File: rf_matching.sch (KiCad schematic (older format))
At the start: 12 parts, among them J1 RFI, J2 RFO, J3 CTRL, J4 ANT, J5 3V3, U1 pe4259ds, U2 SF2098

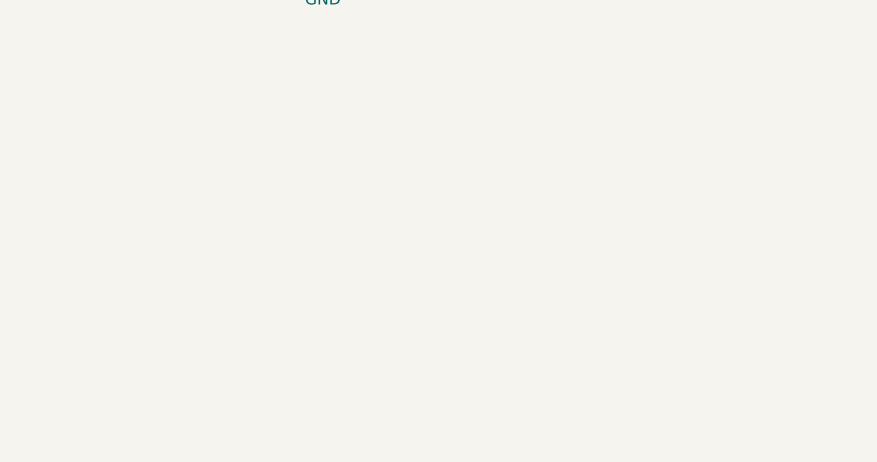
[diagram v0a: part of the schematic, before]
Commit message: Add thicker bias, add PCB LOSS line
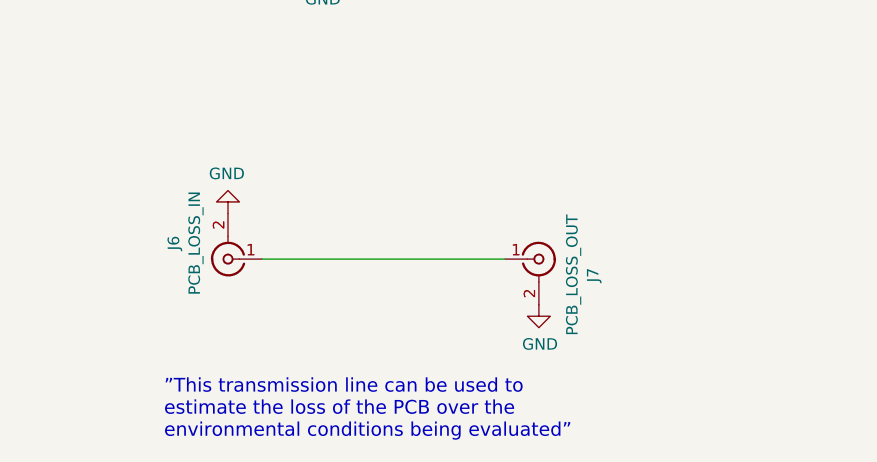
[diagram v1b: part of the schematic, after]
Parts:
- added J6: PCB_LOSS_IN, KiCad/Connectors_Molex.pretty:Molex_SMA_Jack_Edge_Mount, symbol Conn_Coaxial
- added J7: PCB_LOSS_OUT, KiCad/Connectors_Molex.pretty:Molex_SMA_Jack_Edge_Mount, symbol Conn_Coaxial
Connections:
- net GND: now also J6.2 (Ext), J7.2 (Ext)
- new net: J6.1 (In), J7.1 (In)
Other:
- note added: "”This transmission line can be used to \nestimate the loss of the PCB over the \nenvironmental conditions being evaluated”"
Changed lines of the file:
@@
 Wire Wire Line
 	3320 3680 3320 3760
+$Comp
+L Conn_Coaxial J7
+U 1 1 5B8AD0CE
+P 5580 6660
+F 0 "J7" V 5817 6590 50  0000 C CNN
+F 1 "PCB_LOSS_OUT" V 5726 6590 50  0000 C CNN
+F 2 "KiCad/Connectors_Molex.pretty:Molex_SMA_Jack_Edge_Mount" H 5580 6660 50  0001 C CNN
+F 3 "" H 5580 6660 50  0001 C CNN
+	1    5580 6660
+	1    0    0    -1
+$EndComp
+$Comp
+L Conn_Coaxial J6
+U 1 1 5B8AD184
+P 4220 6660
+F 0 "J6" V 4457 6590 50  0000 C CNN
+F 1 "PCB_LOSS_IN" V 4366 6590 50  0000 C CNN
+F 2 "KiCad/Connectors_Molex.pretty:Molex_SMA_Jack_Edge_Mount" H 4220 6660 50  0001 C CNN
+F 3 "" H 4220 6660 50  0001 C CNN
+	1    4220 6660
+	-1   0    0    1
+$EndComp
+Wire Wire Line
+	4370 6660 5430 6660
+$Comp
+L GND #PWR06
+U 1 1 5B8AD8F5
+P 4220 6460
+F 0 "#PWR06" H 4220 6210 50  0001 C CNN
+F 1 "GND" H 4225 6287 50  0000 C CNN
+F 2 "" H 4220 6460 50  0001 C CNN
+F 3 "" H 4220 6460 50  0001 C CNN
+	1    4220 6460
+	-1   0    0    1
+$EndComp
+$Comp
+L GND #PWR07
+U 1 1 5B8ADA42
+P 5580 6860
+F 0 "#PWR07" H 5580 6610 50  0001 C CNN
+F 1 "GND" H 5585 6687 50  0000 C CNN
+F 2 "" H 5580 6860 50  0001 C CNN
+F 3 "" H 5580 6860 50  0001 C CNN
+	1    5580 6860
+	1    0    0    -1
+$EndComp
+Text Notes 3940 7450 0    60   ~ 0
+”This transmission line can be used to \nestimate the loss of the PCB over the \nenvironmental conditions being evaluated”
 $EndSCHEMATC

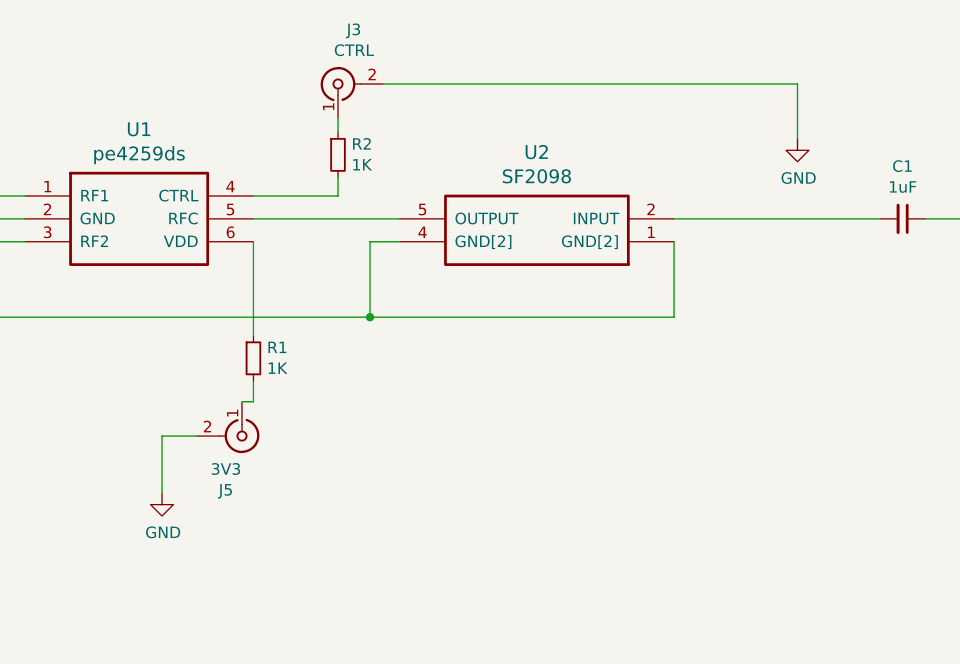
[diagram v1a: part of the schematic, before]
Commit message: Redesign, more similar to official evaluation board
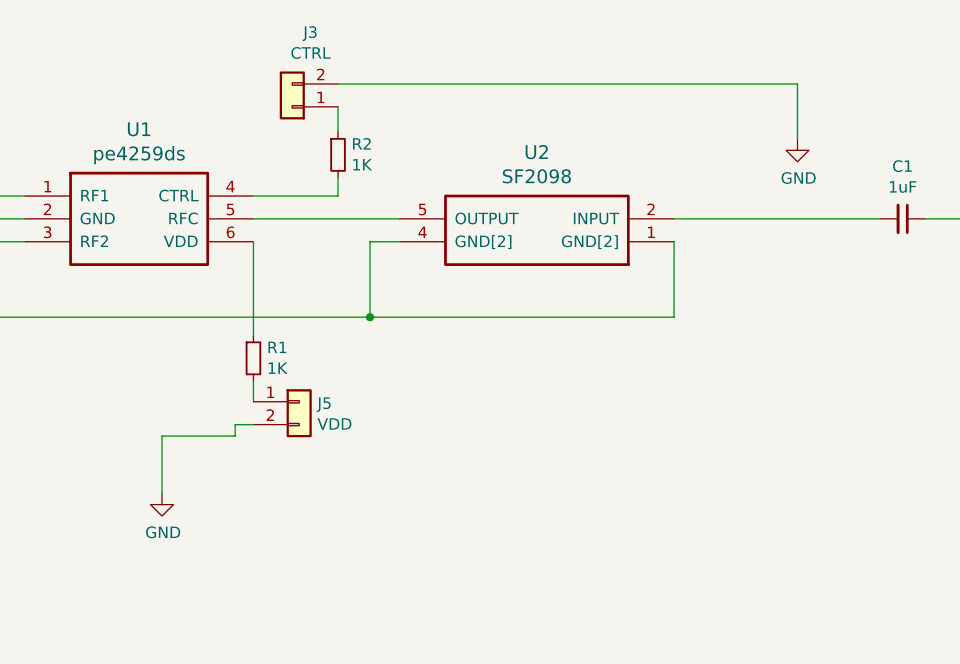
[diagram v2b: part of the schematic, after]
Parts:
- removed J3: CTRL, KiCad/Connectors_Molex.pretty:Molex_SMA_Jack_Edge_Mount, symbol Conn_Coaxial
- removed J5: 3V3, KiCad/Connectors_Molex.pretty:Molex_SMA_Jack_Edge_Mount, symbol Conn_Coaxial
- added J3: CTRL, KiCad/Connectors_Molex.pretty:Molex_KK-6410-02_02x2.54mm_Straight, symbol Conn_01x02
- added J5: VDD, KiCad/Connectors_Molex.pretty:Molex_KK-6410-02_02x2.54mm_Straight, symbol Conn_01x02
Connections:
- net GND: now also J3.2 (Pin_2), J5.2 (Pin_2)
- net at R2.1: now also J3.1 (Pin_1)
- net at R1.2: now also J5.1 (Pin_1)
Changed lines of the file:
@@
-$EndComp
-$Comp
-L Conn_Coaxial J3
-U 1 1 5B4AD06B
-P 5400 3560
-F 0 "J3" V 5637 3490 50  0000 C CNN
-F 1 "CTRL" V 5546 3490 50  0000 C CNN
-F 2 "KiCad/Connectors_Molex.pretty:Molex_SMA_Jack_Edge_Mount" H 5400 3560 50  0001 C CNN
-F 3 "" H 5400 3560 50  0001 C CNN
-	1    5400 3560
-	0    -1   -1   0
 $EndComp
 $Comp
@@
 $EndComp
 $Comp
-L Conn_Coaxial J5
-U 1 1 5B4AF99C
-P 4980 5100
-F 0 "J5" V 5217 5030 50  0000 C CNN
-F 1 "3V3" V 5126 5030 50  0000 C CNN
-F 2 "KiCad/Connectors_Molex.pretty:Molex_SMA_Jack_Edge_Mount" H 4980 5100 50  0001 C CNN
-F 3 "" H 4980 5100 50  0001 C CNN
-	1    4980 5100
-	0    1    1    0
-$EndComp
-$Comp
 L GND #PWR03
 U 1 1 5B4AFA81
@@
 	5030 4050 5400 4050
 Wire Wire Line
-	5600 3560 7410 3560
+	5400 3560 7410 3560
 Wire Wire Line
 	7410 3560 7410 3800
 Wire Wire Line
-	4780 5100 4630 5100
+	4630 5100 4950 5100
 Wire Wire Line
 	4630 5100 4630 5350
 Wire Wire Line
-	5030 4950 4980 4950
-Wire Wire Line
 	5400 4050 5400 3970
 Wire Wire Line
-	5400 3710 5400 3770
-Wire Wire Line
-	5030 4950 5030 4860
+	5400 3660 5400 3770
 Wire Wire Line
 	5030 4660 5030 4250
@@
 Text Notes 3940 7450 0    60   ~ 0
 ”This transmission line can be used to \nestimate the loss of the PCB over the \nenvironmental conditions being evaluated”
+$Comp
+L Conn_01x02 J3
+U 1 1 5B8D137C
+P 5200 3660
+F 0 "J3" H 5120 3335 50  0000 C CNN
+F 1 "CTRL" H 5120 3426 50  0000 C CNN
+F 2 "KiCad/Connectors_Molex.pretty:Molex_KK-6410-02_02x2.54mm_Straight" H 5200 3660 50  0001 C CNN
+F 3 "" H 5200 3660 50  0001 C CNN
+	1    5200 3660
+	-1   0    0    1
+$EndComp
+Wire Wire Line
+	4950 5100 4950 5050
+Wire Wire Line
+	4950 5050 5030 5050
+$Comp
+L Conn_01x02 J5
+U 1 1 5B8D1712
+P 5230 4950
+F 0 "J5" H 5310 4942 50  0000 L CNN
+F 1 "VDD" H 5310 4851 50  0000 L CNN
+F 2 "KiCad/Connectors_Molex.pretty:Molex_KK-6410-02_02x2.54mm_Straight" H 5230 4950 50  0001 C CNN
+F 3 "" H 5230 4950 50  0001 C CNN
+	1    5230 4950
+	1    0    0    -1
+$EndComp
+Wire Wire Line
+	5030 4860 5030 4950
 $EndSCHEMATC
